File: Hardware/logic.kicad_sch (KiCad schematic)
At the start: 84 parts, among them J301 Ref Divider, J303 Encoder, J304 Ref Select, J305 VCO Range, J306 GPS Module, J307 LCD, J308 Serial, J309 RF 50 Ohm, J310 RF TTL, J311 1PPS TTL, J312 Program, J313 ICSP, J314 USB, Q301 2N3904, U301 DAC8571IDGK, U303 OP07, U304 OP07, U306 GALI-52, U307 74LVC1G17, U308 74LVC1G17, U309 MCP23017_SO, U310 MAX232, U311 24AA04, U312 PIC18F27Q43, U313 FT232RL

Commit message: Updated PCB
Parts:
- removed J308: Serial, symbol Connector:DE9_Pins
- added J307: Serial, Connector_PinHeader_2.54mm:PinHeader_1x10_P2.54mm_Vertical, symbol Connector_Generic:Conn_01x10
- C305: renamed from C306; footprint (none) -> Capacitor_THT:CP_Radial_D5.0mm_P2.50mm
- C306: renamed from C307; footprint (none) -> Capacitor_THT:CP_Radial_D5.0mm_P2.50mm
- C307: renamed from C308; footprint (none) -> Capacitor_THT:CP_Radial_D5.0mm_P2.50mm
- C308: renamed from C309; footprint (none) -> Capacitor_THT:CP_Radial_D5.0mm_P2.50mm
- C310: renamed from C311; footprint (none) -> Capacitor_THT:CP_Radial_D5.0mm_P2.50mm
- C311: renamed from C312; footprint (none) -> Capacitor_THT:CP_Radial_D5.0mm_P2.50mm
- C312: renamed from C313; footprint (none) -> Capacitor_THT:C_Disc_D3.0mm_W2.0mm_P2.50mm
- J301: footprint Connector_PinSocket_2.54mm:PinSocket_2x02_P2.54mm_Vertical -> Connector_PinHeader_2.54mm:PinHeader_2x02_P2.54mm_Vertical
- J302: renamed from J303; footprint (none) -> Connector_PinHeader_2.54mm:PinHeader_1x06_P2.54mm_Vertical
- J303: renamed from J304; footprint (none) -> Connector_PinHeader_2.54mm:PinHeader_1x02_P2.54mm_Vertical
- J304: renamed from J306; footprint (none) -> Connector_PinHeader_2.54mm:PinHeader_1x05_P2.54mm_Vertical
- J305: footprint (none) -> Connector_PinHeader_2.54mm:PinHeader_1x03_P2.54mm_Vertical
- J306: renamed from J307; footprint (none) -> Connector_PinHeader_2.54mm:PinHeader_1x14_P2.54mm_Vertical
- J311: renamed from J312; footprint (none) -> Connector_PinHeader_2.54mm:PinHeader_1x02_P2.54mm_Vertical
- J312: renamed from J313; footprint (none) -> Connector_PinHeader_2.54mm:PinHeader_1x05_P2.54mm_Vertical
- J313: renamed from J314; footprint (none) -> Connector_USB:USB_A_Molex_67643_Horizontal
- U308: renamed from U310; footprint (none) -> Package_DIP:DIP-16_W7.62mm_LongPads
- renumbered C302 to C301, C303 to C302, C304 to C303, C305 to C304, C310 to C309, C314 to C313, D302 to D301, D303 to D302, D304 to D303, D305 to D304, D306 to D305, D307 to D306, D308 to D307, D309 to D308, D310 to D309, D311 to D310, D312 to D311, D313 to D312, D314 to D313, J309 to J308, J310 to J309, J311 to J310, R302 to R301, R303 to R302, R304 to R303, R305 to R304, R307 to R305, R308 to R306, R309 to R307, R310 to R308, R316 to R309, R317 to R310, R318 to R311, R319 to R312, R311 to R313, R312 to R314, R313 to R315, R314 to R316, R315 to R317, R320 to R318, R321 to R319, R322 to R320, R323 to R321, U303 to U302, U304 to U303, U306 to U304, U307 to U305, U308 to U306, U309 to U307, U311 to U309, U312 to U310, U313 to U311
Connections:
- net GND: now also J307.5 (Pin_5)
- net RXD: now also J307.2 (Pin_2)
- net TXD: now also J307.3 (Pin_3)
- new net: J307.4 (Pin_4), J307.6 (Pin_6)
- new net: J307.7 (Pin_7), J307.8 (Pin_8)
- no-connect marks 30 -> 31
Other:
- note added: "Pin 9 is polarizing pin"
- note added: "Wire straight pin-to-pin to DB-9 connector except pin 9 which is connected to pin 10 of the board"

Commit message: updated pcb
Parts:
- removed J313: USB, Connector_USB:USB_A_Molex_67643_Horizontal, symbol Connector:USB_B_Micro
- removed U307: MCP23017_SO, Package_SO:SOIC-28W_7.5x17.9mm_P1.27mm, symbol Interface_Expansion:MCP23017_SO
- added J313: USB, Connector_PinSocket_2.54mm:PinSocket_1x05_P2.54mm_Vertical, symbol Connector_Generic:Conn_01x05
- added U308: MCP23017_SO, Package_SO:SOIC-28W_7.5x17.9mm_P1.27mm, symbol DH_Interface:MCP23017_SO
- C301, C303, C304, C309, C313: footprint Capacitor_THT:C_Axial_L3.8mm_D2.6mm_P15.00mm_Horizontal -> Capacitor_THT:C_Axial_L3.8mm_D2.6mm_P7.50mm_Horizontal
- Q301: footprint Package_TO_SOT_THT:TO-92L_HandSolder -> Package_TO_SOT_THT:TO-92_Inline
- renumbered U308 to U307
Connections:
- net +5V: now also U308.9 (VDD)
- net GND: now also J313.4 (Pin_4), J313.5 (Pin_5), U308.10 (VSS), U308.15 (A0), U308.16 (A1), U308.17 (A2)
- net LCD_BL: now also U308.4 (GPB3)
- net LCD_D4: now also U308.5 (GPB4)
- net LCD_D5: now also U308.6 (GPB5)
- net LCD_D6: now also U308.7 (GPB6)
- net LCD_D7: now also U308.8 (GPB7)
- net LCD_E: now also U308.3 (GPB2)
- net LCD_RS: now also U308.1 (GPB0)
- net LCD_RW: now also U308.2 (GPB1)
- net SCL: now also U308.12 (SCK)
- net SDA: now also U308.13 (SDA)
- net ~{RESET}: now also U308.18 (~{RESET})
- net RS232_C1+: now reaches C308.1, U307.1 (C1+)
- net RS232_VS+: now reaches C306.1, U307.2 (VS+)
- net RS232_C1-: now reaches C308.2, U307.3 (C1-)
- net RS232_V-: now reaches C307.2, U307.6 (VS-)
- net at R320.1: now also J313.1 (Pin_1)
- net at U311.16 (USBD-): now also J313.2 (Pin_2)
- net at U311.15 (USBD+): now also J313.3 (Pin_3)
- net FAULT_N renamed LED_Fault
- net LED_Fault: now also U308.24 (GPA3)
- net GPS_N renamed LED_GPS_N
- net LED_GPS_N: now also U308.28 (GPA7)
- net HOLDOVER_N renamed LED_HOLDOVER_N
- net LED_HOLDOVER_N: now also U308.27 (GPA6)
- net LOCK_N renamed LED_LOCK_N
- net LED_LOCK_N: now also U308.26 (GPA5)
- net POWER_N renamed LED_Power
- net LED_Power: now also U308.25 (GPA4)
- no-connect marks 31 -> 33
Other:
- note added: "Red (+5) White (D-) Green (D+) Black (Gnd) Shield (Opt)"
- moved on the sheet: C305, C306, C307, C308, R320, R321, U307

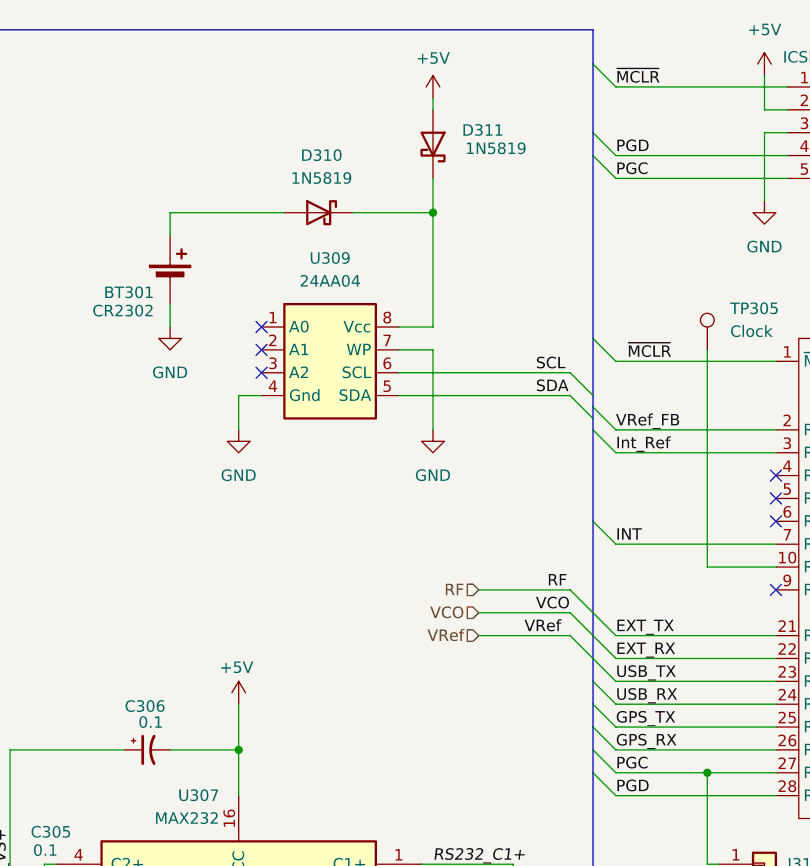
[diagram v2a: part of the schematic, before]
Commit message: Updated Schematic; Move to SMD
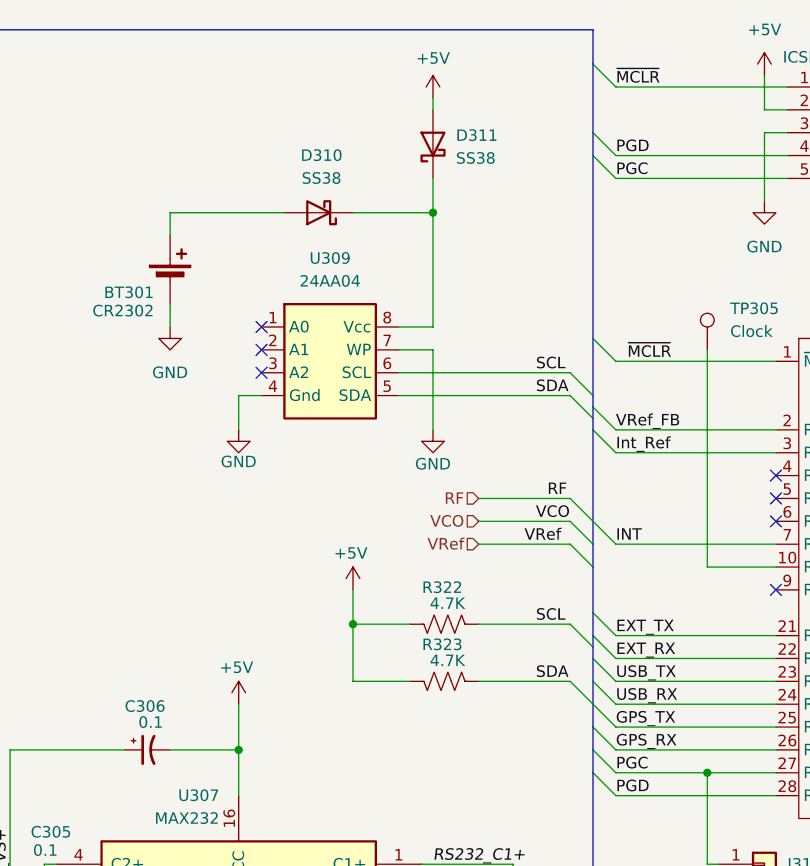
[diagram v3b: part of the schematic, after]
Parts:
- removed D310, D311: 1N5819, Diode_THT:D_DO-41_SOD81_P10.16mm_Horizontal, symbol Diode:1N5819
- added D310, D311: SS38, Diode_SMD:D_SMB_Handsoldering, symbol Diode:SS38
- added R322, R323: 4.7K, Resistor_SMD:R_0805_2012Metric_Pad1.20x1.40mm_HandSolder, symbol Device:R_US
- C301, C303, C304, C309: footprint Capacitor_THT:C_Axial_L3.8mm_D2.6mm_P7.50mm_Horizontal -> Capacitor_SMD:C_0603_1608Metric_Pad1.08x0.95mm_HandSolder
- C302: footprint Capacitor_THT:CP_Radial_D8.0mm_P5.00mm -> Capacitor_SMD:CP_Elec_8x6.9
- C305, C306, C307, C308: footprint Capacitor_THT:CP_Radial_D5.0mm_P2.50mm -> Capacitor_SMD:CP_Elec_4x5.4
- C310: footprint Capacitor_THT:CP_Radial_D5.0mm_P2.50mm -> Capacitor_SMD:CP_Elec_6.3x5.4
- C311: footprint Capacitor_THT:CP_Radial_D5.0mm_P2.50mm -> Capacitor_SMD:CP_Elec_8x6.9
- C312: footprint Capacitor_THT:C_Disc_D3.0mm_W2.0mm_P2.50mm -> Capacitor_SMD:C_0603_1608Metric_Pad1.08x0.95mm_HandSolder
- D301, D302, D303, D304: footprint Diode_SMD:D_SMA -> Diode_SMD:D_SMB_Handsoldering
- FB301, FB302: footprint Ferrite_THT:LairdTech_28C0236-0JW-10 -> Inductor_SMD:L_0805_2012Metric_Pad1.15x1.40mm_HandSolder
- L301: footprint Inductor_THT:L_Axial_L7.0mm_D3.3mm_P10.16mm_Horizontal_Fastron_MICC -> Inductor_SMD:L_1206_3216Metric_Pad1.42x1.75mm_HandSolder
- R301, R302, R303, R304, R305, R306, R307, R308, R309, R310, R311, R312, R313, R314, R315, R316, R317, R318, R319, R320, R321: footprint Resistor_THT:R_Axial_DIN0204_L3.6mm_D1.6mm_P7.62mm_Horizontal -> Resistor_SMD:R_0805_2012Metric_Pad1.20x1.40mm_HandSolder
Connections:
- net +5V: now also D311.2 (A), R322.1, R323.1
- net SCL: now also R322.2
- net SDA: now also R323.2
- net at BT301.1 (+): now also D310.2 (A)
- net at U309.8 (Vcc): now also D310.1 (K), D311.1 (K)

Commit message: updated pcb
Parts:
- BT301: value CR2302 -> CR2032
- C313: footprint Capacitor_THT:C_Axial_L3.8mm_D2.6mm_P7.50mm_Horizontal -> Capacitor_SMD:C_0603_1608Metric_Pad1.08x0.95mm_HandSolder
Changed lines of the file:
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@@
 			)
 		)
-		(property "Value" "CR2302"
+		(property "Value" "CR2032"
 			(at 258.064 47.752 0)
 			(effects
@@
 			)
 		)
-		(property "Footprint" "Capacitor_THT:C_Axial_L3.8mm_D2.6mm_P7.50mm_Horizontal"
+		(property "Footprint" "Capacitor_SMD:C_0603_1608Metric_Pad1.08x0.95mm_HandSolder"
 			(at 382.27 165.1 0)
 			(effects

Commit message: Updated PCB
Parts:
- C304: value 0.1 -> 100n
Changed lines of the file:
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@@
 			)
 		)
-		(property "Value" "0.1"
+		(property "Value" "100n"
 			(at 196.088 27.686 0)
 			(effects

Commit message: updated pcb
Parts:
- removed J301: Ref Divider, Connector_PinHeader_2.54mm:PinHeader_2x02_P2.54mm_Vertical, symbol Connector_Generic:Conn_02x02_Odd_Even
- added J314: Ref Select, Connector_PinHeader_2.54mm:PinHeader_1x03_P2.54mm_Vertical, symbol Connector_Generic:Conn_01x03
- added JP301: EXT_TX, Resistor_THT:R_Box_L26.0mm_W5.0mm_P20.00mm, symbol Jumper:Jumper_2_Bridged
- added JP302: EXT_RX, Resistor_THT:R_Box_L26.0mm_W5.0mm_P20.00mm, symbol Jumper:Jumper_2_Bridged
- J303: footprint Connector_PinHeader_2.54mm:PinHeader_1x02_P2.54mm_Vertical -> Connector_PinHeader_2.54mm:PinHeader_1x03_P2.54mm_Vertical
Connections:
- net IntRef is gone; now on net Int_Ref: J303.3 (Pin_3)
- net EXT_RX: now also JP302.2 (B); no longer U307.12 (R1OUT)
- net EXT_TX: now also JP301.2 (B); no longer U307.11 (T1IN)
- net VRef: now also J314.2 (Pin_2)
- net at R301.1, R302.2, U302.3 (+): now also J314.1 (Pin_1)
- net at R301.2: now also J314.3 (Pin_3)
- new net: JP301.1 (A), U307.11 (T1IN)
- new net: JP302.1 (A), U307.12 (R1OUT)
- no-connect marks 33 -> 37
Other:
- moved on the sheet: C305, C306, C307, U307

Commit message: finished pcb drc edits
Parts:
- Q301: footprint Package_TO_SOT_THT:TO-92_Inline -> Package_TO_SOT_THT:TO-92L_HandSolder
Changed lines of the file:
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@@
 			)
 		)
-		(property "Footprint" "Package_TO_SOT_THT:TO-92_Inline"
+		(property "Footprint" "Package_TO_SOT_THT:TO-92L_HandSolder"
 			(at 167.64 219.075 0)
 			(effects
